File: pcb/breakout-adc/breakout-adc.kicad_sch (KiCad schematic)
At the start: 23 parts, among them J1 Screw_Terminal_01x04, J10 Conn_01x01_Pin, J11 Conn_01x12_Pin, J12 Conn_01x12_Pin, J13 Conn_01x01_Pin, J14 Conn_01x01_Pin, J15 FX18-120P-0.8SV20, J2 Screw_Terminal_01x02, J3 Conn_01x01_Pin, J4 Conn_01x01_Pin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

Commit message: [adc][pcb] adc jumper select silks
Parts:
- U8, U9: footprint digikey-footprints:SOT-363 -> D1213A:SOT-363_DIO
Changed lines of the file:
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@@
 			)
 		)
-		(property "Footprint" "digikey-footprints:SOT-363"
+		(property "Footprint" "D1213A:SOT-363_DIO"
 			(at 111.76 46.99 0)
 			(effects
@@
 			)
 		)
-		(property "Footprint" "digikey-footprints:SOT-363"
+		(property "Footprint" "D1213A:SOT-363_DIO"
 			(at 111.76 97.79 0)
 			(effects

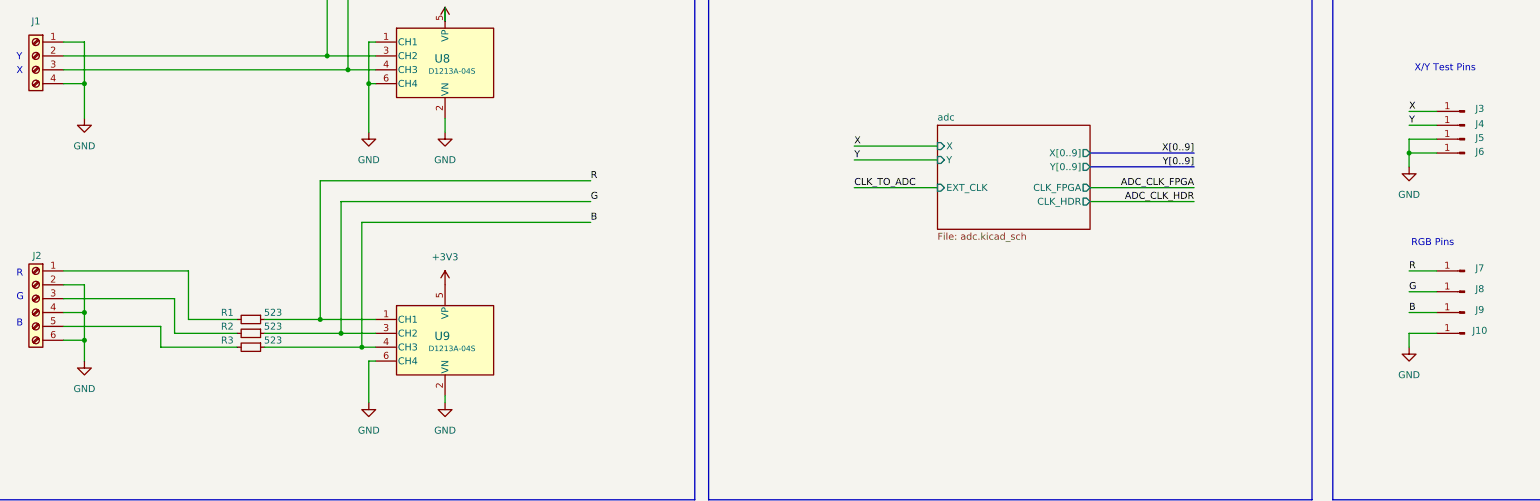
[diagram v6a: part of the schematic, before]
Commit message: [adc][pcb] improve ergonomics of test points
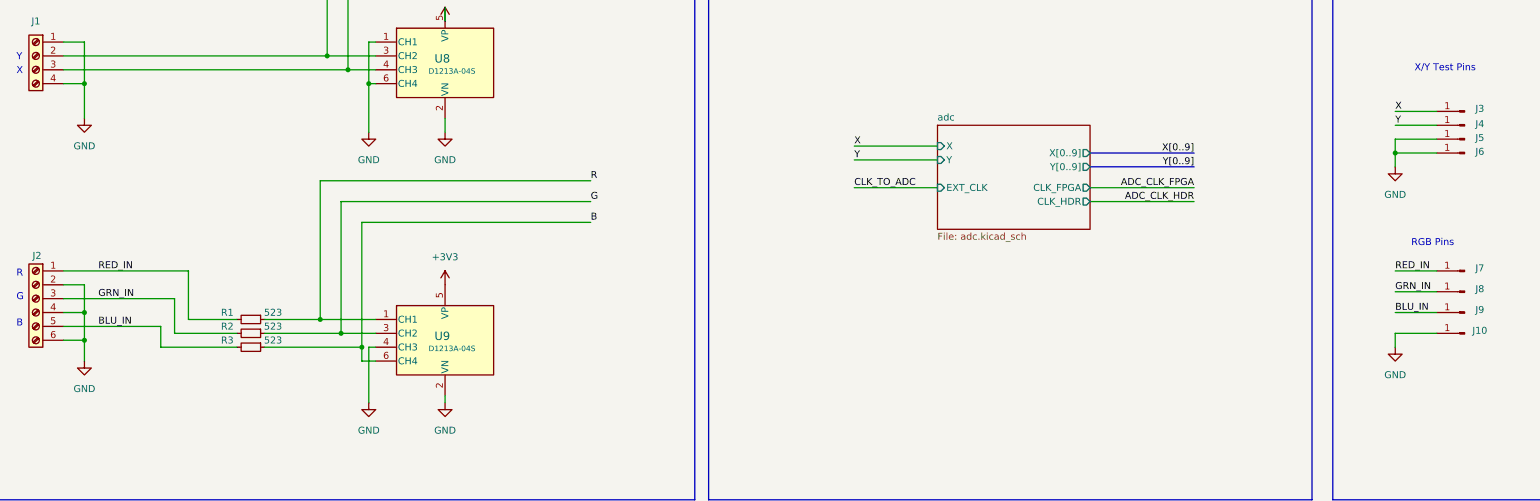
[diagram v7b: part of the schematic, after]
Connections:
- net B: now also U9.6 (CH4); no longer J9.1 (Pin_1), U9.4 (CH3)
- net G: no longer J8.1 (Pin_1)
- net GND: now also U9.4 (CH3); no longer U9.6 (CH4)
- net R: no longer J7.1 (Pin_1)
- net RED_IN: now reaches J2.1 (Pin_1), R1.2
- net RED_IN: now also J7.1 (Pin_1)
- net BLU_IN: now reaches J2.5 (Pin_5), R3.2
- net BLU_IN: now also J9.1 (Pin_1)
- net GRN_IN: now reaches J2.3 (Pin_3), R2.2
- net GRN_IN: now also J8.1 (Pin_1)
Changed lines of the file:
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@@
 	)
 	(junction
+		(at 96.52 99.06)
+		(diameter 0)
+		(color 0 0 0 0)
+	)
+	(junction
 		(at 127 246.38)
 		(diameter 0)
@@
 	)
 	(junction
-		(at 288.29 63.5)
+		(at 285.75 63.5)
 		(diameter 0)
 		(color 0 0 0 0)
@@
 	)
 	(junction
-		(at 96.52 99.06)
-		(diameter 0)
-		(color 0 0 0 0)
-	)
-	(junction
 		(at 127 243.84)
 		(diameter 0)
@@
 	(wire
 		(pts
+			(xy 96.52 99.06) (xy 96.52 101.6)
+		)
+		(stroke
+			(width 0)
+			(type default)
+		)
+	)
+	(wire
+		(pts
 			(xy 127 243.84) (xy 123.19 243.84)
 		)
@@
 	(wire
 		(pts
-			(xy 293.37 88.9) (xy 288.29 88.9)
+			(xy 285.75 88.9) (xy 293.37 88.9)
 		)
 		(stroke
@@
 	(wire
 		(pts
-			(xy 288.29 96.52) (xy 288.29 99.06)
+			(xy 285.75 96.52) (xy 285.75 99.06)
 		)
 		(stroke
@@
 	(wire
 		(pts
-			(xy 293.37 63.5) (xy 288.29 63.5)
+			(xy 293.37 63.5) (xy 285.75 63.5)
 		)
 		(stroke
@@
 	(wire
 		(pts
-			(xy 288.29 60.96) (xy 288.29 63.5)
+			(xy 285.75 60.96) (xy 285.75 63.5)
 		)
 		(stroke
@@
 	(wire
 		(pts
-			(xy 293.37 92.71) (xy 288.29 92.71)
+			(xy 293.37 92.71) (xy 285.75 92.71)
 		)
 		(stroke
@@
 	(wire
 		(pts
-			(xy 293.37 85.09) (xy 288.29 85.09)
+			(xy 293.37 85.09) (xy 285.75 85.09)
+		)
+		(stroke
+			(width 0)
+			(type default)
+		)
+	)
+	(wire
+		(pts
+			(xy 78.74 99.06) (xy 96.52 99.06)
 		)
 		(stroke
@@
 	(wire
 		(pts
-			(xy 293.37 55.88) (xy 288.29 55.88)
+			(xy 293.37 55.88) (xy 285.75 55.88)
 		)
 		(stroke
@@
 	(wire
 		(pts
-			(xy 288.29 96.52) (xy 293.37 96.52)
+			(xy 285.75 96.52) (xy 293.37 96.52)
 		)
 		(stroke
@@
 	(wire
 		(pts
-			(xy 96.52 99.06) (xy 99.06 99.06)
-		)
-		(stroke
-			(width 0)
-			(type default)
-		)
-	)
-	(wire
-		(pts
 			(xy 90.17 27.94) (xy 90.17 45.72)
 		)
@@
 	(wire
 		(pts
-			(xy 97.79 101.6) (xy 97.79 109.22)
-		)
-		(stroke
-			(width 0)
-			(type default)
-		)
-	)
-	(wire
-		(pts
 			(xy 45.72 43.18) (xy 45.72 50.8)
 		)
@@
 	(wire
 		(pts
-			(xy 78.74 99.06) (xy 96.52 99.06)
-		)
-		(stroke
-			(width 0)
-			(type default)
-		)
-	)
-	(wire
-		(pts
 			(xy 97.79 43.18) (xy 97.79 50.8)
 		)
@@
 	(wire
 		(pts
-			(xy 288.29 63.5) (xy 288.29 66.04)
+			(xy 285.75 63.5) (xy 285.75 66.04)
 		)
 		(stroke
@@
 		)
 	)
+	(bus
+		(pts
+			(xy 229.87 63.5) (xy 248.92 63.5)
+		)
+		(stroke
+			(width 0)
+			(type default)
+		)
+	)
 	(wire
 		(pts
-			(xy 97.79 101.6) (xy 99.06 101.6)
+			(xy 186.69 64.77) (xy 201.93 64.77)
 		)
 		(stroke
@@
 		)
 	)
-	(bus
+	(wire
 		(pts
-			(xy 229.87 63.5) (xy 248.92 63.5)
+			(xy 123.19 193.04) (xy 146.05 193.04)
 		)
 		(stroke
@@
 	(wire
 		(pts
-			(xy 186.69 64.77) (xy 201.93 64.77)
+			(xy 346.71 78.74) (xy 363.22 78.74)
 		)
 		(stroke
@@
 	(wire
 		(pts
-			(xy 123.19 193.04) (xy 146.05 193.04)
+			(xy 97.79 99.06) (xy 99.06 99.06)
 		)
 		(stroke
@@
 	(wire
 		(pts
-			(xy 346.71 78.74) (xy 363.22 78.74)
+			(xy 99.06 101.6) (xy 96.52 101.6)
+		)
+		(stroke
+			(width 0)
+			(type default)
+		)
+	)
+	(wire
+		(pts
+			(xy 97.79 99.06) (xy 97.79 109.22)
 		)
 		(stroke
@@
 	(wire
 		(pts
-			(xy 293.37 60.96) (xy 288.29 60.96)
+			(xy 293.37 60.96) (xy 285.75 60.96)
 		)
 		(stroke
@@
 	(wire
 		(pts
-			(xy 293.37 58.42) (xy 288.29 58.42)
+			(xy 293.37 58.42) (xy 285.75 58.42)
 		)
 		(stroke
@@
 		)
 	)
+	(label "GRN_IN"
+		(at 48.26 90.17 0)
+		(fields_autoplaced yes)
+		(effects
+			(font
+				(size 1.27 1.27)
+			)
+			(justify left bottom)
+		)
+	)
 	(label "GND"
 		(at 96.52 160.02 180)
@@
 		)
 	)
-	(label "R"
-		(at 288.29 85.09 0)
+	(label "RED_IN"
+		(at 285.75 85.09 0)
 		(fields_autoplaced yes)
 		(effects
@@
 		)
 	)
-	(label "G"
-		(at 288.29 88.9 0)
+	(label "RED_IN"
+		(at 48.26 85.09 0)
+		(fields_autoplaced yes)
+		(effects
+			(font
+				(size 1.27 1.27)
+			)
+			(justify left bottom)
+		)
+	)
+	(label "GRN_IN"
+		(at 285.75 88.9 0)
 		(fields_autoplaced yes)
 		(effects
@@
 	)
 	(label "X"
-		(at 288.29 55.88 0)
+		(at 285.75 55.88 0)
 		(fields_autoplaced yes)
 		(effects
@@
 		)
 	)
+	(label "BLU_IN"
+		(at 48.26 95.25 0)
+		(fields_autoplaced yes)
+		(effects
+			(font
+				(size 1.27 1.27)
+			)
+			(justify left bottom)
+		)
+	)
 	(label "B"
 		(at 144.78 160.02 0)
@@
 		)
 	)
-	(label "B"
-		(at 288.29 92.71 0)
+	(label "BLU_IN"
+		(at 285.75 92.71 0)
 		(fields_autoplaced yes)
 		(effects
@@
 	)
 	(label "Y"
-		(at 288.29 58.42 0)
+		(at 285.75 58.42 0)
 		(fields_autoplaced yes)
 		(effects
@@
 	(symbol
 		(lib_id "power:GND")
-		(at 288.29 66.04 0)
+		(at 285.75 66.04 0)
 		(mirror y)
 		(unit 1)
@@
 		(fields_autoplaced yes)
 		(property "Reference" "#PWR0101"
-			(at 288.29 72.39 0)
+			(at 285.75 72.39 0)
 			(effects
 				(font
@@
 		)
 		(property "Value" "GND"
-			(at 288.29 71.12 0)
+			(at 285.75 71.12 0)
 			(effects
 				(font
@@
 		)
 		(property "Footprint" ""
-			(at 288.29 66.04 0)
+			(at 285.75 66.04 0)
 			(effects
 				(font
@@
 		)
 		(property "Datasheet" ""
-			(at 288.29 66.04 0)
+			(at 285.75 66.04 0)
 			(effects
 				(font
@@
 		)
 		(property "Description" "Power symbol creates a global label with name \"GND\" , ground"
-			(at 288.29 66.04 0)
+			(at 285.75 66.04 0)
 			(effects
 				(font
@@
 	(symbol
 		(lib_id "power:GND")
-		(at 288.29 99.06 0)
+		(at 285.75 99.06 0)
 		(mirror y)
 		(unit 1)
@@
 		(fields_autoplaced yes)
 		(property "Reference" "#PWR0102"
-			(at 288.29 105.41 0)
+			(at 285.75 105.41 0)
 			(effects
 				(font
@@
 		)
 		(property "Value" "GND"
-			(at 288.29 104.14 0)
+			(at 285.75 104.14 0)
 			(effects
 				(font
@@
 		)
 		(property "Footprint" ""
-			(at 288.29 99.06 0)
+			(at 285.75 99.06 0)
 			(effects
 				(font
@@
 		)
 		(property "Datasheet" ""
-			(at 288.29 99.06 0)
+			(at 285.75 99.06 0)
 			(effects
 				(font
@@
 		)
 		(property "Description" "Power symbol creates a global label with name \"GND\" , ground"
-			(at 288.29 99.06 0)
+			(at 285.75 99.06 0)
 			(effects
 				(font

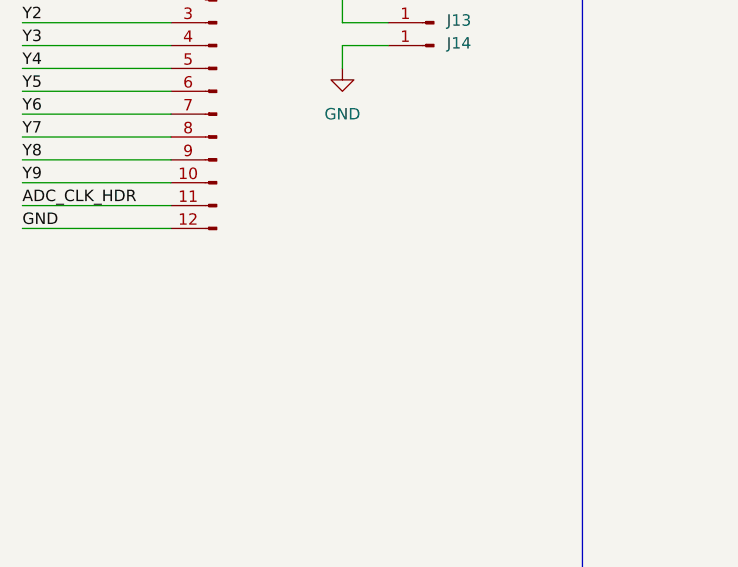
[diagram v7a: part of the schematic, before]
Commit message: [adc][pcb] add more gnd test points
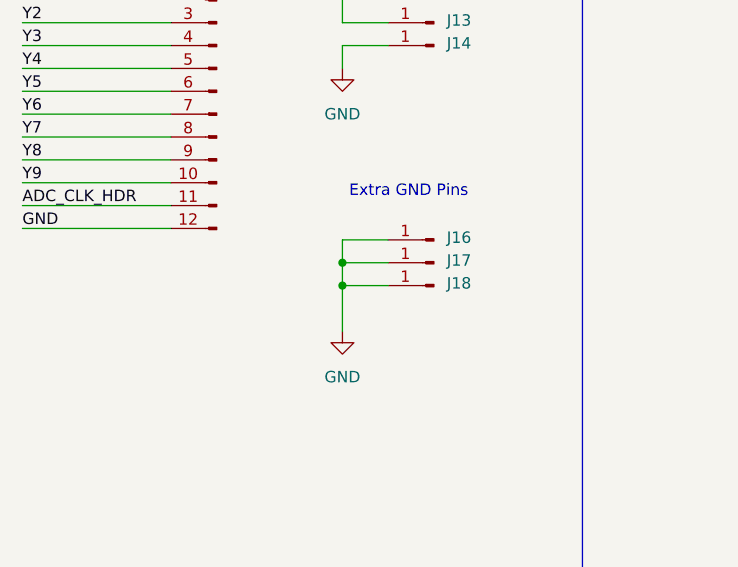
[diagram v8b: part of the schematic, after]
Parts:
- added J16, J17, J18: Conn_01x01_Pin, TestPoint:TestPoint_Keystone_5000-5004_Miniature, symbol Connector:Conn_01x01_Pin
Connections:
- net GND: now also J16.1 (Pin_1), J17.1 (Pin_1), J18.1 (Pin_1)
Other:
- note added: "Extra GND Pins"
